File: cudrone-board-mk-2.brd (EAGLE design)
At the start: 100 x 70 mm, 169 parts, among them U1 EDISON_CONNECTOR_FULLMOUNTING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, U10 A2235-H, U11 FTS31XS-U, U12 BNO055, U13 DSPIC33EP512MU810-X_PF, U2 FTS31XS-U, U4 TPS62065, U5 USD-SOCKETNEW, U6 TXB0108, U8 PCA9306, U9 PCA9306

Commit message: Added reset to mcu
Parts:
- removed RESET: SWITCH-MOMENTARY-2PTH, SparkFun-Electromechanical:TACTILE-PTH
- added C47: 0.1uF, SparkFun-Capacitors:0603-CAP
- added EDISON_RESET, MCU_RESET: SWITCH-MOMENTARY-2, SparkFun-Electromechanical:EVQPSC02K
- added R63: 470, SparkFun-Resistors:0603
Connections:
- new net MCLR: R63.1, U13.13
- new net N$45: C47.1, MCU_RESET.A, MCU_RESET.A'
- net GND: now also C47.2, EDISON_RESET.B, EDISON_RESET.B'; no longer RESET.3
- net N$15: now also EDISON_RESET.A, EDISON_RESET.A'; no longer RESET.1
- net VPP: now also MCU_RESET.B, MCU_RESET.B', R63.2; no longer U13.13
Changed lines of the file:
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@@
 </autorouter>
 <elements>
-<element name="U$1" library="frames" package="LETTER_L" value="" x="-75.5" y="-59"/>
-<element name="U$2" library="frames" package="DOCFIELD" value="" x="71.5" y="-59"/>
+<element name="U$1" library="frames" library_urn="urn:adsk.eagle:library:229" package="LETTER_L" value="" x="-75.5" y="-59"/>
+<element name="U$2" library="frames" library_urn="urn:adsk.eagle:library:229" package="DOCFIELD" value="" x="71.5" y="-59"/>
 <element name="U1" library="SparkFun-Boards" package="EDISON_DAUGHTER" value="EDISON_CONNECTOR_FULLMOUNTING_HOLES" x="32" y="49" rot="R270"/>
 <element name="BAT_BACKUP" library="SparkFun-Electromechanical" package="BATTCON_12MM" value="RTC backup battery" x="-66" y="-67"/>
@@
 <element name="POWER" library="SparkFun-Electromechanical" package="JS102011SAQN-SPDT" value="CANSAT_SWITCH" x="-77" y="-362"/>
 <element name="U10" library="A2235-H" package="XCVR_A2235-H" value="A2235-H" x="-96" y="-358"/>
-<element name="RESET" library="SparkFun-Electromechanical" package="TACTILE-PTH" value="SWITCH-MOMENTARY-2PTH" x="-93" y="-382"/>
 <element name="R15" library="SparkFun-Resistors" package="0603-RES@1" value="10K" x="-103" y="-402">
 <attribute name="PROD_ID" value="RES-00824" x="-103" y="-395" size="1.778" layer="27" display="off"/>
@@
 <element name="C45" library="SparkFun-Passives" package="0805" value="47 uF" x="-141" y="-816"/>
 <element name="C46" library="SparkFun-Passives" package="0805" value="47 uF" x="-144" y="-816"/>
+<element name="R63" library="SparkFun-Resistors" package="0603" value="470" x="-142" y="-820">
+<attribute name="PROD_ID" value="RES-09334" x="-142" y="-820" size="1.778" layer="27" display="off"/>
+</element>
+<element name="EDISON_RESET" library="SparkFun-Electromechanical" package="EVQPSC02K" value="SWITCH-MOMENTARY-2" x="-154" y="-817"/>
+<element name="C47" library="SparkFun-Capacitors" package="0603-CAP" value="0.1uF" x="-154" y="-823">
+<attribute name="PROD_ID" value="CAP-00810" x="-154" y="-823" size="1.778" layer="27" display="off"/>
+</element>
+<element name="MCU_RESET" library="SparkFun-Electromechanical" package="EVQPSC02K" value="SWITCH-MOMENTARY-2" x="-162" y="-820"/>
 </elements>
 <signals>
@@
 <contactref element="U10" pad="29"/>
 <contactref element="U10" pad="30"/>
-<contactref element="RESET" pad="3"/>
 <contactref element="POWER" pad="P$3"/>
 <contactref element="U9" pad="4"/>
@@
 <contactref element="C45" pad="2"/>
 <contactref element="C46" pad="2"/>
+<contactref element="EDISON_RESET" pad="B"/>
+<contactref element="EDISON_RESET" pad="B'"/>
+<contactref element="C47" pad="2"/>
 <wire x1="-91.3175" y1="-412.3203" x2="-90.6825" y2="-417.6797" width="0" layer="19" extent="1-1"/>
 <wire x1="-98.275" y1="-418.3" x2="-90.6825" y2="-417.6797" width="0" layer="19" extent="1-1"/>
@@
 <wire x1="-103.23" y1="-398.4462" x2="-101" y2="-413.315" width="0" layer="19" extent="1-1"/>
 <wire x1="-98.15" y1="-395" x2="-103.23" y2="-398.4462" width="0" layer="19" extent="1-1"/>
-<wire x1="-96.2512" y1="-384.2606" x2="-98.15" y2="-395" width="0" layer="19" extent="1-1"/>
-<wire x1="-104" y1="-365.62" x2="-96.2512" y2="-384.2606" width="0" layer="19" extent="1-1"/>
+<wire x1="-104" y1="-365.62" x2="-98.15" y2="-395" width="0" layer="19" extent="1-1"/>
 <wire x1="-99.81" y1="-363.715" x2="-104" y2="-365.62" width="0" layer="19" extent="1-1"/>
 <wire x1="-97.27" y1="-363.715" x2="-99.81" y2="-363.715" width="0" layer="19" extent="1-1"/>
@@
 <wire x1="-140.1" y1="-816" x2="-137.1" y2="-816" width="0" layer="19" extent="1-1"/>
 <wire x1="-143.1" y1="-816" x2="-140.1" y2="-816" width="0" layer="19" extent="1-1"/>
+<wire x1="-152.3" y1="-814.85" x2="-143.1" y2="-816" width="0" layer="19" extent="1-1"/>
+<wire x1="-152.2" y1="-819.15" x2="-152.3" y2="-814.85" width="0" layer="19" extent="1-1"/>
+<wire x1="-153.15" y1="-823" x2="-152.2" y2="-819.15" width="0" layer="19" extent="1-1"/>
 <wire x1="48.37" y1="47.02" x2="-66" y2="-67" width="0" layer="19" extent="1-1"/>
 <wire x1="48.77" y1="47.02" x2="48.37" y2="47.02" width="0" layer="19" extent="1-1"/>
@@
 <contactref element="U13" pad="16"/>
 <contactref element="U13" pad="2"/>
-<contactref element="ICSP" pad="5"/>
 <contactref element="R61" pad="2"/>
 <contactref element="C24" pad="2"/>
@@
 <contactref element="C45" pad="1"/>
 <contactref element="C46" pad="1"/>
+<contactref element="ICSP" pad="5"/>
 <wire x1="-102.15" y1="-402" x2="-102.15" y2="-405" width="0" layer="19" extent="1-1"/>
 <wire x1="-96.15" y1="-402" x2="-102.15" y2="-402" width="0" layer="19" extent="1-1"/>
@@
 <contactref element="R9" pad="2"/>
 <contactref element="R8" pad="2"/>
-<contactref element="RESET" pad="1"/>
-<wire x1="-73.15" y1="-132" x2="-96.2512" y2="-379.7394" width="0" layer="19" extent="1-1"/>
+<contactref element="EDISON_RESET" pad="A"/>
+<contactref element="EDISON_RESET" pad="A'"/>
+<wire x1="-155.7" y1="-814.85" x2="-155.7" y2="-819.15" width="0" layer="19" extent="1-1"/>
+<wire x1="-73.15" y1="-132" x2="-155.7" y2="-814.85" width="0" layer="19" extent="1-1"/>
 <wire x1="-69.15" y1="-128" x2="-73.15" y2="-132" width="0" layer="19" extent="1-1"/>
 </signal>
@@
 <signal name="VPP">
 <contactref element="ICSP" pad="6"/>
-<contactref element="U13" pad="13"/>
 <contactref element="R61" pad="1"/>
+<contactref element="R63" pad="2"/>
+<contactref element="MCU_RESET" pad="B"/>
+<contactref element="MCU_RESET" pad="B'"/>
+<wire x1="-160.3" y1="-817.85" x2="-160.2" y2="-822.15" width="0" layer="19" extent="1-1"/>
+<wire x1="-141.15" y1="-820" x2="-160.2" y2="-822.15" width="0" layer="19" extent="1-1"/>
+<wire x1="-118.85" y1="-723" x2="-141.15" y2="-820" width="0" layer="19" extent="1-1"/>
 <wire x1="-103.65" y1="-714.81" x2="-118.85" y2="-723" width="0" layer="19" extent="1-1"/>
-<wire x1="-117.62" y1="-693" x2="-103.65" y2="-714.81" width="0" layer="19" extent="1-1"/>
 </signal>
 <signal name="PGD">
@@
 <contactref element="R62" pad="5"/>
 </signal>
+<signal name="MCLR">
+<contactref element="U13" pad="13"/>
+<contactref element="R63" pad="1"/>
+<wire x1="-117.62" y1="-693" x2="-142.85" y2="-820" width="0" layer="19" extent="1-1"/>
+</signal>
+<signal name="N$45">
+<contactref element="MCU_RESET" pad="A"/>
+<contactref element="MCU_RESET" pad="A'"/>
+<contactref element="C47" pad="1"/>
+<wire x1="-163.7" y1="-817.85" x2="-163.7" y2="-822.15" width="0" layer="19" extent="1-1"/>
+<wire x1="-154.85" y1="-823" x2="-163.7" y2="-822.15" width="0" layer="19" extent="1-1"/>
+</signal>
 </signals>

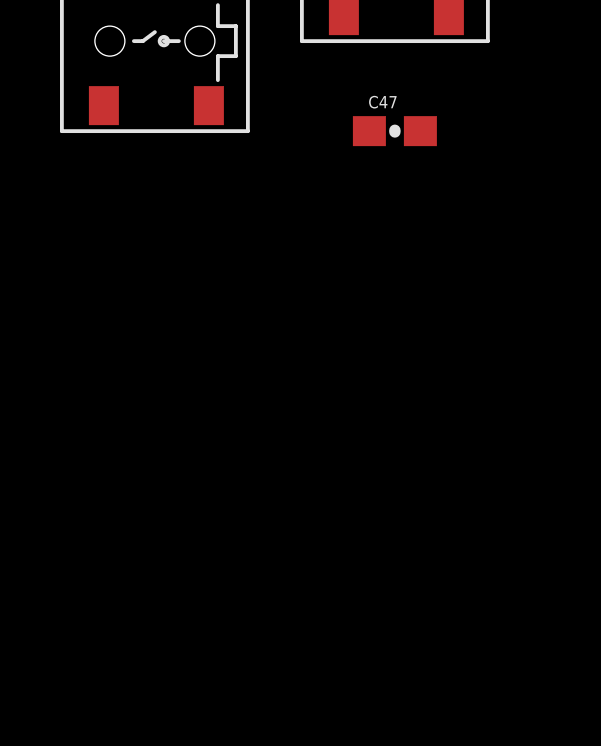
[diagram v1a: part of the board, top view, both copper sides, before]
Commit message: Added resinator to mcu
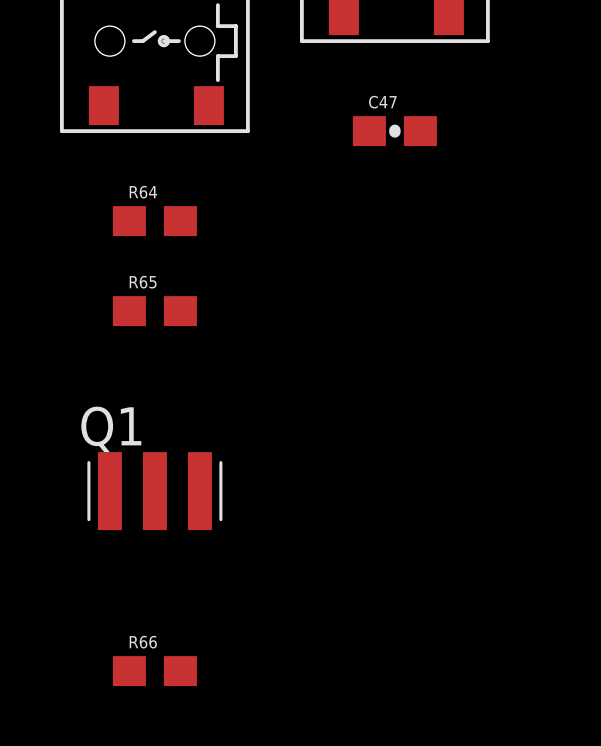
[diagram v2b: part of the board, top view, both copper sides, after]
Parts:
- added Q1: CSTCR6M00G53Z, murata-filter:CSTCR6M
- added R64, R65: 50, SparkFun-Resistors:0603
- added R66: 1M, SparkFun-Resistors:0603
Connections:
- new net N$46: ICSP.3, R64.2
- new net N$47: ICSP.2, R65.2
- new net OSC1: Q1.3, R66.2, U13.63
- new net OSC2: Q1.1, R66.1, U13.64
- net GND: now also Q1.2
- net PGC: now also R65.1; no longer ICSP.2
- net PGD: now also R64.1; no longer ICSP.3
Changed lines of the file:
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@@
 </element>
 <element name="MCU_RESET" library="SparkFun-Electromechanical" package="EVQPSC02K" value="SWITCH-MOMENTARY-2" x="-162" y="-820"/>
+<element name="R64" library="SparkFun-Resistors" package="0603" value="50" x="-162" y="-826">
+<attribute name="PROD_ID" value="RES-09334" x="-162" y="-826" size="1.778" layer="27" display="off"/>
+</element>
+<element name="R65" library="SparkFun-Resistors" package="0603" value="50" x="-162" y="-829">
+<attribute name="PROD_ID" value="RES-09334" x="-162" y="-829" size="1.778" layer="27" display="off"/>
+</element>
+<element name="Q1" library="murata-filter" package="CSTCR6M" value="CSTCR6M00G53Z" x="-162" y="-835">
+<attribute name="MF" value="" x="-170" y="-826" size="1.778" layer="27" display="off"/>
+<attribute name="MPN" value="CSTCR6M00G53-R0" x="-170" y="-826" size="1.778" layer="27" display="off"/>
+<attribute name="OC_FARNELL" value="1170434" x="-170" y="-826" size="1.778" layer="27" display="off"/>
+<attribute name="OC_NEWARK" value="25M8759" x="-170" y="-826" size="1.778" layer="27" display="off"/>
+</element>
+<element name="R66" library="SparkFun-Resistors" package="0603" value="1M" x="-162" y="-841">
+<attribute name="PROD_ID" value="RES-09334" x="-162" y="-841" size="1.778" layer="27" display="off"/>
+</element>
 </elements>
 <signals>
@@
 <contactref element="EDISON_RESET" pad="B'"/>
 <contactref element="C47" pad="2"/>
+<contactref element="Q1" pad="2"/>
 <wire x1="-91.3175" y1="-412.3203" x2="-90.6825" y2="-417.6797" width="0" layer="19" extent="1-1"/>
 <wire x1="-98.275" y1="-418.3" x2="-90.6825" y2="-417.6797" width="0" layer="19" extent="1-1"/>
@@
 <wire x1="-152.2" y1="-819.15" x2="-152.3" y2="-814.85" width="0" layer="19" extent="1-1"/>
 <wire x1="-153.15" y1="-823" x2="-152.2" y2="-819.15" width="0" layer="19" extent="1-1"/>
+<wire x1="-162" y1="-835" x2="-153.15" y2="-823" width="0" layer="19" extent="1-1"/>
 <wire x1="48.37" y1="47.02" x2="-66" y2="-67" width="0" layer="19" extent="1-1"/>
 <wire x1="48.77" y1="47.02" x2="48.37" y2="47.02" width="0" layer="19" extent="1-1"/>
@@
 </signal>
 <signal name="PGD">
-<contactref element="ICSP" pad="3"/>
 <contactref element="U13" pad="27"/>
-<wire x1="-115.4999875" y1="-700.62" x2="-111.27" y2="-714.81" width="0" layer="19" extent="1-1"/>
+<contactref element="R64" pad="1"/>
+<wire x1="-115.4999875" y1="-700.62" x2="-162.85" y2="-826" width="0" layer="19" extent="1-1"/>
 </signal>
 <signal name="PGC">
-<contactref element="ICSP" pad="2"/>
 <contactref element="U13" pad="26"/>
-<wire x1="-115.9999875" y1="-700.62" x2="-113.81" y2="-714.81" width="0" layer="19" extent="1-1"/>
+<contactref element="R65" pad="1"/>
+<wire x1="-115.9999875" y1="-700.62" x2="-162.85" y2="-829" width="0" layer="19" extent="1-1"/>
 </signal>
 <signal name="LVP">
@@
 <wire x1="-154.85" y1="-823" x2="-163.7" y2="-822.15" width="0" layer="19" extent="1-1"/>
 </signal>
+<signal name="N$46">
+<contactref element="ICSP" pad="3"/>
+<contactref element="R64" pad="2"/>
+<wire x1="-111.27" y1="-714.81" x2="-161.15" y2="-826" width="0" layer="19" extent="1-1"/>
+</signal>
+<signal name="N$47">
+<contactref element="ICSP" pad="2"/>
+<contactref element="R65" pad="2"/>
+<wire x1="-113.81" y1="-714.81" x2="-161.15" y2="-829" width="0" layer="19" extent="1-1"/>
+</signal>
+<signal name="OSC2">
+<contactref element="U13" pad="64"/>
+<contactref element="Q1" pad="1"/>
+<contactref element="R66" pad="1"/>
+<wire x1="-163.5" y1="-835" x2="-162.85" y2="-841" width="0" layer="19" extent="1-1"/>
+<wire x1="-102.38" y1="-692.5" x2="-163.5" y2="-835" width="0" layer="19" extent="1-1"/>
+</signal>
+<signal name="OSC1">
+<contactref element="U13" pad="63"/>
+<contactref element="Q1" pad="3"/>
+<contactref element="R66" pad="2"/>
+<wire x1="-160.5" y1="-835" x2="-161.15" y2="-841" width="0" layer="19" extent="1-1"/>
+<wire x1="-102.38" y1="-693" x2="-160.5" y2="-835" width="0" layer="19" extent="1-1"/>
+</signal>
 </signals>

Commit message: Added longer pin headers for servos and connected io to mcu
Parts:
- removed GIMBAL_SERVOS1: 3X4, Drone_Connectors:3X4
- removed JP4: (no value), SparkFun-Connectors:1X03
- added RECIVER: 3X8, Drone_Connectors:3X8
- ESC, MOTOR_SERVO: value 3X6 -> 3X10; device Drone_Connectors:3X6 -> Drone_Connectors:3X10
- JP3: device SparkFun-Connectors:1X03 -> SparkFun-Connectors:2X3-DOUBLE-JUMPER-SWAP
- moved ESC 561.4 mm to (-144.0, -877.0)
- moved MOTOR_SERVO 561.4 mm to (-144.0, -901.0)
- moved JP3 248.6 mm to (-153.0, -854.0)
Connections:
- new net AUX_1: RECIVER.S4, U13.41
- new net AUX_2: RECIVER.S3, U13.42
- new net AUX_3: RECIVER.S2, U13.43
- new net AUX_4: RECIVER.S1, U13.44
- new net M10: ESC.S1, U13.52
- new net M7: ESC.S4, U13.77
- new net M8: ESC.S3, U13.76
- new net M9: ESC.S2, U13.53
- new net MS10: MOTOR_SERVO.S1, U13.78
- new net MS7: MOTOR_SERVO.S4, U13.10
- new net MS8: MOTOR_SERVO.S3, U13.49
- new net MS9: MOTOR_SERVO.S2, U13.50
- net 5V: now also ESC.V10, ESC.V7, ESC.V8, ESC.V9, MOTOR_SERVO.V10, MOTOR_SERVO.V7, MOTOR_SERVO.V8, MOTOR_SERVO.V9, RECIVER.V1, RECIVER.V2, RECIVER.V3, RECIVER.V4, RECIVER.V5, RECIVER.V6, RECIVER.V7, RECIVER.V8; no longer GIMBAL_SERVOS1.V1, GIMBAL_SERVOS1.V2, GIMBAL_SERVOS1.V3, GIMBAL_SERVOS1.V4
- net CON_RX: now also JP3.1; no longer JP4.1
- net CON_TX: now also JP3.2; no longer JP3.1
- net GND: now also ESC.G10, ESC.G7, ESC.G8, ESC.G9, MOTOR_SERVO.G10, MOTOR_SERVO.G7, MOTOR_SERVO.G8, MOTOR_SERVO.G9, RECIVER.G1, RECIVER.G2, RECIVER.G3, RECIVER.G4, RECIVER.G5, RECIVER.G6, RECIVER.G7, RECIVER.G8; no longer GIMBAL_SERVOS1.G1, GIMBAL_SERVOS1.G2, GIMBAL_SERVOS1.G3, GIMBAL_SERVOS1.G4
- net GP134_UART_2_RX: now also JP3.4; no longer JP3.2
- net GP135_UART_2_TX: now also JP3.3; no longer JP4.2
- net M1: now also ESC.S10, U13.100; no longer ESC.S6
- net M2: now also ESC.S9, U13.98; no longer ESC.S5
- net M3: now also ESC.S8, U13.93; no longer ESC.S4
- net M4: now also ESC.S7, U13.3; no longer ESC.S3
- net M5: now also ESC.S6, U13.5; no longer ESC.S2
- net M6: now also ESC.S5, U13.4; no longer ESC.S1
- net MS1: now also MOTOR_SERVO.S10, U13.99; no longer MOTOR_SERVO.S6
- net MS2: now also MOTOR_SERVO.S9, U13.94; no longer MOTOR_SERVO.S5
- net MS3: now also MOTOR_SERVO.S8, U13.6; no longer MOTOR_SERVO.S4
- net MS4: now also MOTOR_SERVO.S7, U13.7; no longer MOTOR_SERVO.S3
- net MS5: now also MOTOR_SERVO.S6, U13.8; no longer MOTOR_SERVO.S2
- net MS6: now also MOTOR_SERVO.S5, U13.9; no longer MOTOR_SERVO.S1
- net PITCH: now also RECIVER.S8, U13.11; no longer GIMBAL_SERVOS1.S4
- net ROLL: now also RECIVER.S7, U13.12; no longer GIMBAL_SERVOS1.S3
- net THROTTLE: now also RECIVER.S5, U13.25; no longer GIMBAL_SERVOS1.S1
- net XBEE_RX_LOW: now also JP3.5; no longer JP4.3
- net XBEE_TX_LOW: now also JP3.6; no longer JP3.3
- net YAW: now also RECIVER.S6, U13.24; no longer GIMBAL_SERVOS1.S2
